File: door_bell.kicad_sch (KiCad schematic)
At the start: 79 parts, among them J1 Power, J2 Speaker, J3 SWITCH1, J4 UART, J5 MicroSD, J6 Door panel, K1 HJR 1-2C, Q1 BC847, SW1 Reset, SW2 Boot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

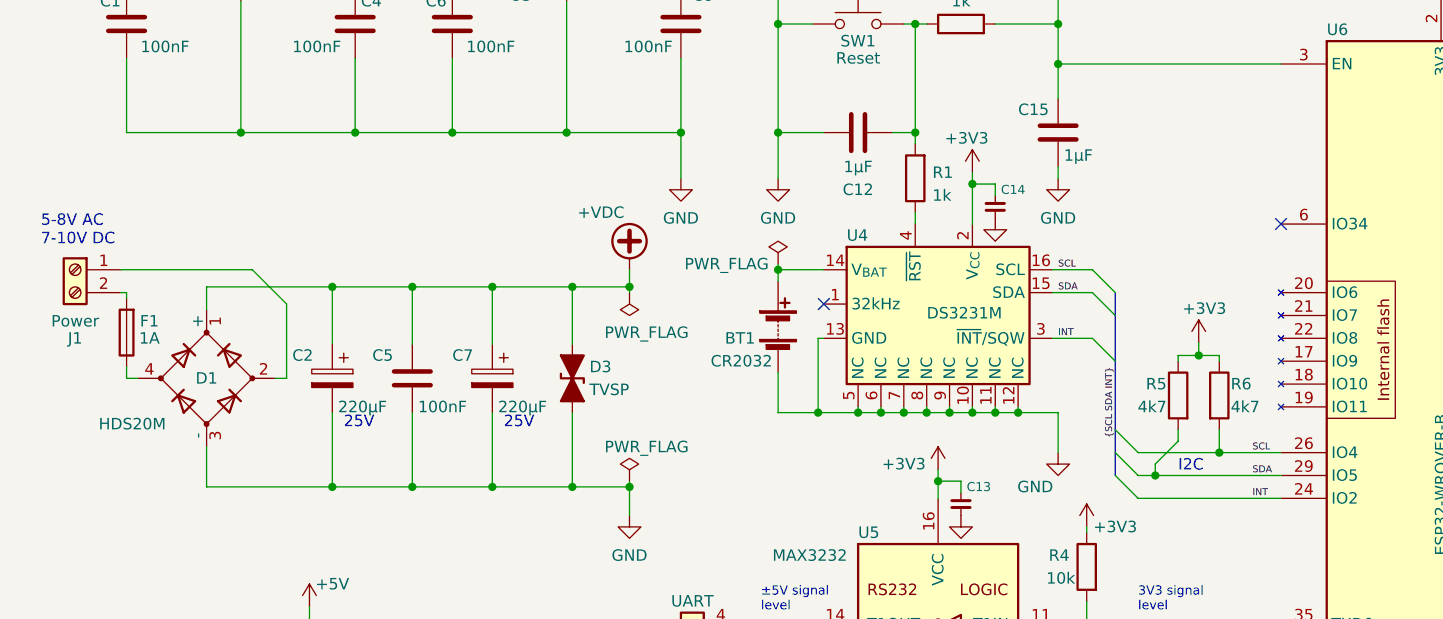
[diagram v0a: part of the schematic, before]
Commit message: Downscale fuse to 500 mA slow-blow after tests
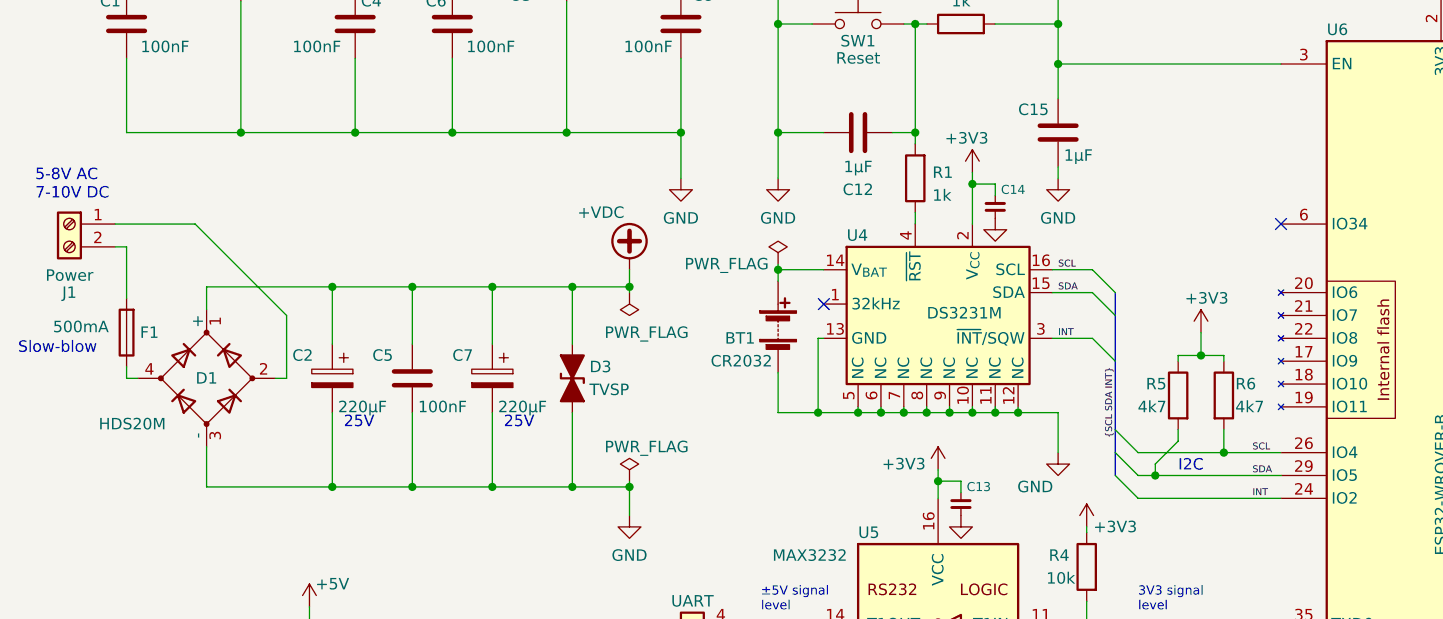
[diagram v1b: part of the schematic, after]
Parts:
- F1: value 1A -> 500mA
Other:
- note added: "Slow-blow"
- moved on the sheet: J1, R6
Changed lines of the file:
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@@
   (junction (at 201.93 134.62) (diameter 0) (color 0 0 0 0)
   )
-  (junction (at 149.606 75.565) (diameter 0) (color 0 0 0 0)
-  )
   (junction (at 213.36 127) (diameter 0) (color 0 0 0 0)
   )
@@
   (junction (at 217.17 151.13) (diameter 0) (color 0 0 0 0)
   )
+  (junction (at 149.86 75.565) (diameter 0) (color 0 0 0 0)
+  )
   (junction (at 86.36 67.945) (diameter 0) (color 0 0 0 0)
   )
@@
   (junction (at 79.375 50.8) (diameter 0) (color 0 0 0 0)
   )
+  (junction (at 152.4 86.36) (diameter 0) (color 0 0 0 0)
+  )
   (junction (at 233.045 151.13) (diameter 0) (color 0 0 0 0)
   )
@@
   (junction (at 30.48 28.575) (diameter 0) (color 0 0 0 0)
   )
-  (junction (at 151.892 86.36) (diameter 0) (color 0 0 0 0)
-  )
   (junction (at 240.665 102.235) (diameter 0) (color 0 0 0 0)
   )
@@
     (stroke (width 0) (type default))
   )
+  (wire (pts (xy 147.32 75.565) (xy 149.86 75.565))
+    (stroke (width 0) (type default))
+  )
   (wire (pts (xy 222.25 147.955) (xy 222.25 151.13))
     (stroke (width 0) (type default))
@@
     (stroke (width 0) (type default))
   )
+  (wire (pts (xy 149.86 75.565) (xy 152.4 75.565))
+    (stroke (width 0) (type default))
+  )
   (wire (pts (xy 222.25 70.485) (xy 222.25 71.12))
     (stroke (width 0) (type default))
@@
     (stroke (width 0) (type default))
   )
-  (wire (pts (xy 29.845 68.58) (xy 30.48 68.58))
+  (wire (pts (xy 29.21 63.5) (xy 30.48 63.5))
     (stroke (width 0) (type default))
   )
@@
     (stroke (width 0) (type default))
   )
-  (wire (pts (xy 151.892 86.36) (xy 158.75 86.36))
+  (wire (pts (xy 142.875 86.36) (xy 152.4 86.36))
     (stroke (width 0) (type default))
   )
@@
     (stroke (width 0) (type default))
   )
+  (wire (pts (xy 152.4 86.36) (xy 158.75 86.36))
+    (stroke (width 0) (type default))
+  )
   (polyline (pts (xy 267.208 43.18) (xy 267.97 43.688))
     (stroke (width 0) (type default))
@@
     (stroke (width 0) (type default))
   )
-  (wire (pts (xy 151.892 83.82) (xy 151.892 86.36))
-    (stroke (width 0) (type default))
-  )
   (wire (pts (xy 86.36 66.04) (xy 86.36 67.945))
     (stroke (width 0) (type default))
@@
     (stroke (width 0) (type default))
   )
+  (wire (pts (xy 152.4 83.82) (xy 152.4 86.36))
+    (stroke (width 0) (type default))
+  )
   (wire (pts (xy 102.87 66.04) (xy 107.95 66.04))
     (stroke (width 0) (type default))
@@
     (stroke (width 0) (type default))
   )
-  (wire (pts (xy 149.606 75.565) (xy 151.892 75.565))
-    (stroke (width 0) (type default))
-  )
   (wire (pts (xy 133.35 66.04) (xy 137.795 66.04))
     (stroke (width 0) (type default))
@@
     (stroke (width 0) (type default))
   )
-  (wire (pts (xy 48.26 69.85) (xy 48.26 78.105))
-    (stroke (width 0) (type default))
-  )
   (wire (pts (xy 39.37 67.945) (xy 53.34 67.945))
     (stroke (width 0) (type default))
@@
     (stroke (width 0) (type default))
   )
-  (wire (pts (xy 29.845 66.04) (xy 44.45 66.04))
+  (wire (pts (xy 29.21 60.96) (xy 38.1 60.96))
     (stroke (width 0) (type default))
   )
@@
     (stroke (width 0) (type default))
   )
-  (wire (pts (xy 44.45 66.04) (xy 48.26 69.85))
-    (stroke (width 0) (type default))
-  )
   (wire (pts (xy 30.48 28.575) (xy 30.48 34.925))
     (stroke (width 0) (type default))
@@
     (stroke (width 0) (type default))
   )
-  (wire (pts (xy 30.48 68.58) (xy 30.48 69.215))
+  (wire (pts (xy 30.48 63.5) (xy 30.48 69.215))
     (stroke (width 0) (type default))
   )
@@
     (stroke (width 0) (type default))
   )
+  (wire (pts (xy 38.1 60.96) (xy 48.26 71.12))
+    (stroke (width 0) (type default))
+  )
   (wire (pts (xy 111.76 81.915) (xy 114.3 81.915))
     (stroke (width 0) (type default))
   )
-  (wire (pts (xy 149.606 74.168) (xy 149.606 75.565))
+  (wire (pts (xy 149.86 73.025) (xy 149.86 75.565))
     (stroke (width 0) (type default))
   )
@@
     (stroke (width 0) (type default))
   )
-  (wire (pts (xy 151.892 75.565) (xy 151.892 76.2))
+  (wire (pts (xy 152.4 75.565) (xy 152.4 76.2))
     (stroke (width 0) (type default))
   )
@@
     (stroke (width 0) (type default))
   )
-  (wire (pts (xy 149.606 75.565) (xy 147.32 75.565))
-    (stroke (width 0) (type default))
-  )
   (wire (pts (xy 48.26 142.24) (xy 48.26 144.78))
     (stroke (width 0) (type default))
@@
     (stroke (width 0) (type default))
   )
+  (wire (pts (xy 48.26 71.12) (xy 48.26 78.105))
+    (stroke (width 0) (type default))
+  )
   (wire (pts (xy 55.88 50.8) (xy 66.675 50.8))
     (stroke (width 0) (type default))
@@
     (stroke (width 0) (type default))
   )
-  (wire (pts (xy 142.875 86.36) (xy 151.892 86.36))
-    (stroke (width 0) (type default))
-  )
   (wire (pts (xy 147.32 132.08) (xy 158.75 132.08))
     (stroke (width 0) (type default))
@@
     (effects (font (size 1.016 1.016)) (justify left bottom))
   )
-  (text "5-8V AC\n7-10V DC" (at 20.955 63.5 0)
+  (text "5-8V AC\n7-10V DC" (at 20.32 58.42 0)
+    (effects (font (size 1.27 1.27)) (justify left bottom))
+  )
+  (text "Slow-blow" (at 18.415 75.565 0)
     (effects (font (size 1.27 1.27)) (justify left bottom))
   )
@@
     )
   )
-  (symbol (lib_id "Connector:Screw_Terminal_01x02") (at 24.765 66.04 0) (mirror y) (unit 1)
+  (symbol (lib_id "Connector:Screw_Terminal_01x02") (at 24.13 60.96 0) (mirror y) (unit 1)
     (in_bom yes) (on_board yes) (dnp no)
-    (property "Reference" "J1" (at 24.765 73.66 0)
+    (property "Reference" "J1" (at 24.13 68.58 0)
       (effects (font (size 1.27 1.27)))
     )
-    (property "Value" "Power" (at 24.765 71.755 0)
+    (property "Value" "Power" (at 24.13 66.675 0)
       (effects (font (size 1.27 1.27)))
     )
-    (property "Footprint" "TerminalBlock_Phoenix_espena:TerminalBlock_Phoenix_PT-1,5-2-3.5-H_1x02_P3.50mm_Horizontal_stackable" (at 24.765 66.04 0)
+    (property "Footprint" "TerminalBlock_Phoenix_espena:TerminalBlock_Phoenix_PT-1,5-2-3.5-H_1x02_P3.50mm_Horizontal_stackable" (at 24.13 60.96 0)
       (effects (font (size 1.27 1.27)) hide)
     )
-    (property "Datasheet" "~" (at 24.765 66.04 0)
+    (property "Datasheet" "~" (at 24.13 60.96 0)
       (effects (font (size 1.27 1.27)) hide)
     )
@@
     )
   )
-  (symbol (lib_id "power:+3V3") (at 149.606 74.168 0) (mirror y) (unit 1)
+  (symbol (lib_id "power:+3V3") (at 149.86 73.025 0) (mirror y) (unit 1)
     (in_bom yes) (on_board yes) (dnp no)
-    (property "Reference" "#PWR026" (at 149.606 77.978 0)
+    (property "Reference" "#PWR026" (at 149.86 76.835 0)
       (effects (font (size 1.27 1.27)) hide)
     )
-    (property "Value" "+3V3" (at 150.241 70.358 0)
+    (property "Value" "+3V3" (at 150.495 69.215 0)
       (effects (font (size 1.27 1.27)))
     )
-    (property "Footprint" "" (at 149.606 74.168 0)
+    (property "Footprint" "" (at 149.86 73.025 0)
       (effects (font (size 1.27 1.27)) hide)
     )
-    (property "Datasheet" "" (at 149.606 74.168 0)
+    (property "Datasheet" "" (at 149.86 73.025 0)
       (effects (font (size 1.27 1.27)) hide)
     )
@@
     )
   )
-  (symbol (lib_id "Device:R") (at 151.892 80.01 0) (unit 1)
+  (symbol (lib_id "Device:R") (at 152.4 80.01 0) (unit 1)
     (in_bom yes) (on_board yes) (dnp no)
-    (property "Reference" "R6" (at 153.162 78.74 0)
+    (property "Reference" "R6" (at 153.67 78.74 0)
       (effects (font (size 1.27 1.27)) (justify left))
     )
-    (property "Value" "4k7" (at 153.162 81.28 0)
+    (property "Value" "4k7" (at 153.67 81.28 0)
       (effects (font (size 1.27 1.27)) (justify left))
     )
-    (property "Footprint" "Resistor_SMD:R_0805_2012Metric_Pad1.20x1.40mm_HandSolder" (at 150.114 80.01 90)
+    (property "Footprint" "Resistor_SMD:R_0805_2012Metric_Pad1.20x1.40mm_HandSolder" (at 150.622 80.01 90)
       (effects (font (size 1.27 1.27)) hide)
     )
-    (property "Datasheet" "~" (at 151.892 80.01 0)
+    (property "Datasheet" "~" (at 152.4 80.01 0)
       (effects (font (size 1.27 1.27)) hide)
     )
@@
   (symbol (lib_id "Device:Fuse") (at 30.48 73.025 180) (unit 1)
     (in_bom yes) (on_board yes) (dnp no)
-    (property "Reference" "F1" (at 33.02 71.755 0)
+    (property "Reference" "F1" (at 33.02 73.025 0)
       (effects (font (size 1.27 1.27)))
     )
-    (property "Value" "1A" (at 33.02 73.66 0)
+    (property "Value" "500mA" (at 25.4 72.39 0)
       (effects (font (size 1.27 1.27)))
     )

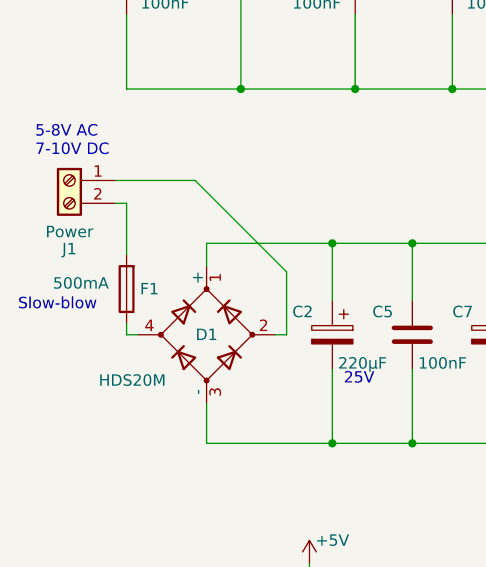
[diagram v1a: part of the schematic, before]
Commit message: Downscale fuse F1 to 250 mA after testing
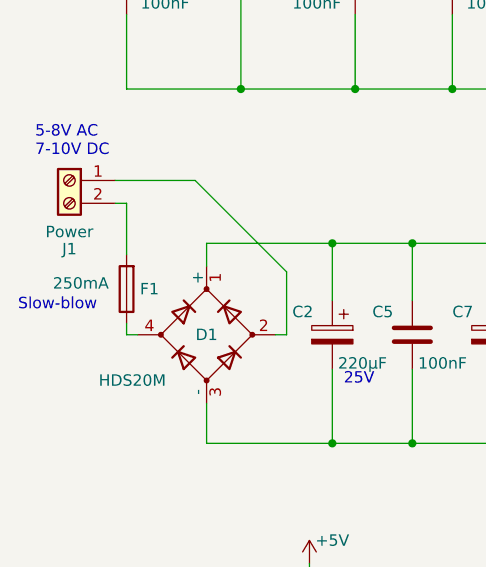
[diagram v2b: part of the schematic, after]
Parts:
- F1: value 500mA -> 250mA
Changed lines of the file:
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@@
       (effects (font (size 1.27 1.27)))
     )
-    (property "Value" "500mA" (at 25.4 72.39 0)
+    (property "Value" "250mA" (at 25.4 72.39 0)
       (effects (font (size 1.27 1.27)))
     )

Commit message: PCB artwork for version 1.2
Implementing changes for new version. Added two decoupling capacitors to SD card, improved thermal relief for 5V regulator and connected RTC _INT/SQW pin from RTC. Copper pours on outer layers.
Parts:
- U1: footprint Package_TO_SOT_SMD:SOT-223-3_TabPin2 -> Package_TO_SOT_SMD_espena:SOT-223-3_ThermalPad_TabPin2
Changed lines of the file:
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@@
       (effects (font (size 1.27 1.27)))
     )
-    (property "Footprint" "Package_TO_SOT_SMD:SOT-223-3_TabPin2" (at 43.18 23.495 0)
+    (property "Footprint" "Package_TO_SOT_SMD_espena:SOT-223-3_ThermalPad_TabPin2" (at 43.18 23.495 0)
       (effects (font (size 1.27 1.27)) hide)
     )

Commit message: Add heatsink to 5V regulator
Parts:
- U1: footprint Package_TO_SOT_SMD_espena:SOT-223-3_ThermalPad_TabPin2 -> Package_TO_SOT_SMD_espena:SOT-223-3_TabPin2_ThermalPads_Heatsink
- U3: footprint Package_TO_SOT_SMD:SOT-223-3_TabPin2 -> Package_TO_SOT_SMD_espena:SOT-223-3_TabPin2_ThermalPads
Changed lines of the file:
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@@
       (effects (font (size 1.27 1.27)))
     )
-    (property "Footprint" "Package_TO_SOT_SMD:SOT-223-3_TabPin2" (at 79.375 23.495 0)
+    (property "Footprint" "Package_TO_SOT_SMD_espena:SOT-223-3_TabPin2_ThermalPads" (at 79.375 23.495 0)
       (effects (font (size 1.27 1.27)) hide)
     )
@@
       (effects (font (size 1.27 1.27)))
     )
-    (property "Footprint" "Package_TO_SOT_SMD_espena:SOT-223-3_ThermalPad_TabPin2" (at 43.18 23.495 0)
-      (effects (font (size 1.27 1.27)) hide)
-    )
+    (property "Footprint" "Package_TO_SOT_SMD_espena:SOT-223-3_TabPin2_ThermalPads_Heatsink" (at 43.18 23.495 0)
+      (effects (font (size 1.27 1.27)) hide)
+    )

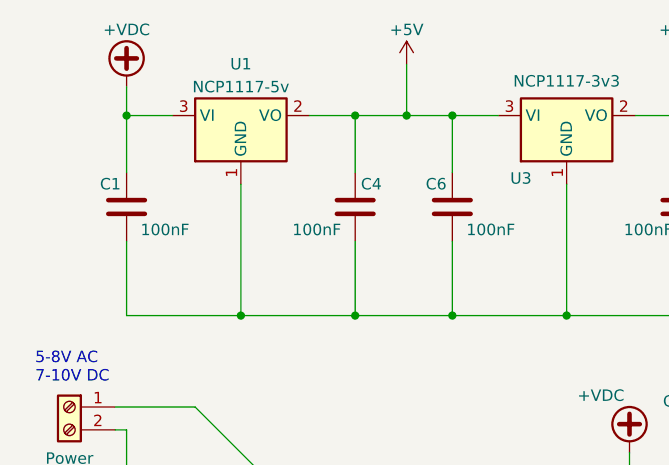
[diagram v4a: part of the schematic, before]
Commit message: Add 'hot surface' symbol to 5V regulator
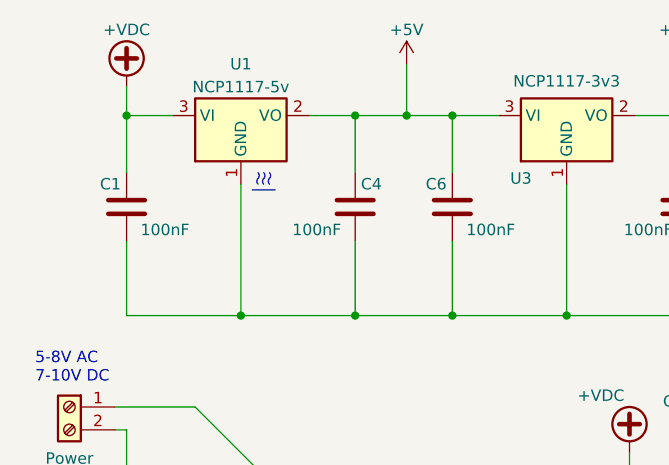
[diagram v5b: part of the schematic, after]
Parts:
- U1: footprint Package_TO_SOT_SMD_espena:SOT-223-3_TabPin2_ThermalPads_Heatsink -> Package_TO_SOT_SMD_espena:SOT-223-3_TabPin2_ThermalPads_Heatsink_x2
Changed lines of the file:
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@@
+    (stroke (width 0) (type default))
+  )
+  (polyline (pts (xy 44.45 36.83) (xy 46.99 36.83))
     (stroke (width 0) (type default))
   )
@@
   (wire (pts (xy 39.37 90.17) (xy 53.34 90.17))
     (stroke (width 0) (type default))
+  )
+  (arc (start 45.72 34.925) (mid 45.8515 35.2425) (end 45.72 35.56)
+    (stroke (width 0) (type default))
+    (fill (type none))
+  )
+  (arc (start 45.085 36.195) (mid 44.9535 35.8775) (end 45.085 35.56)
+    (stroke (width 0) (type default))
+    (fill (type none))
+  )
+  (arc (start 45.72 36.195) (mid 45.5885 35.8775) (end 45.72 35.56)
+    (stroke (width 0) (type default))
+    (fill (type none))
+  )
+  (arc (start 45.085 34.925) (mid 45.2165 35.2425) (end 45.085 35.56)
+    (stroke (width 0) (type default))
+    (fill (type none))
+  )
+  (arc (start 46.355 34.925) (mid 46.484 35.2418) (end 46.355 35.56)
+    (stroke (width 0) (type default))
+    (fill (type none))
+  )
+  (arc (start 46.355 36.195) (mid 46.226 35.8782) (end 46.355 35.56)
+    (stroke (width 0) (type default))
+    (fill (type none))
   )
   (text "TXD" (at 88.9 108.585 0)
@@
       (effects (font (size 1.27 1.27)))
     )
-    (property "Footprint" "Package_TO_SOT_SMD_espena:SOT-223-3_TabPin2_ThermalPads_Heatsink" (at 43.18 23.495 0)
-      (effects (font (size 1.27 1.27)) hide)
-    )
+    (property "Footprint" "Package_TO_SOT_SMD_espena:SOT-223-3_TabPin2_ThermalPads_Heatsink_x2" (at 43.18 23.495 0)
+      (effects (font (size 1.27 1.27)) hide)
+    )
